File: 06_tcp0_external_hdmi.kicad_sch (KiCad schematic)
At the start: 27 parts, among them J30 External HDMI-A from TCP0, U50 TPD4E02B04DQA HDMI2.0 TMDS ES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, U51 TPD4E02B04DQA HDMI2.0 TMDS ES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, U52 TPD4E02B04DQA HDMI sideband E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

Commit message: Publish the current Ducktop2 design
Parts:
- removed F150: 100mA HDMI 5V detect fuse, Fuse:Fuse_1206_3216Metric, symbol Device:Fuse
- removed U51: TPD4E02B04DQA HDMI2.0 TMDS ESD B, Package_SON:USON-10_2.5x1.0mm_P0.5mm, symbol Power_Protection:TPD4E02B04DQA
- removed U52: TPD4E02B04DQA HDMI sideband ESD, Package_SON:USON-10_2.5x1.0mm_P0.5mm, symbol Power_Protection:TPD4E02B04DQA
- added C156, C157: 100n 16V HDMI AC coupling, Capacitor_SMD:C_0402_1005Metric, symbol Device:C
- added C159: 1u 10V X7R HDMI 5V switch output, Capacitor_SMD:C_0805_2012Metric, symbol Device:C
- added C160: 100p PCA9306 VREF2/EN filter, Capacitor_SMD:C_0402_1005Metric, symbol Device:C
- added C161: 100n HPD buffer local, Capacitor_SMD:C_0402_1005Metric, symbol Device:C
- added C162: 100n 10V X7R HDMI 5V switch input HF, Capacitor_SMD:C_0402_1005Metric, symbol Device:C
- added C163: 100n 10V X7R HDMI 5V switch output HF, Capacitor_SMD:C_0402_1005Metric, symbol Device:C
- added C164: 4.7n HDMI 5V switch rise-time, Capacitor_SMD:C_0402_1005Metric, symbol Device:C
- added C165: 4.7n HDMI 3V3 switch rise-time, Capacitor_SMD:C_0402_1005Metric, symbol Device:C
- added D155, D156, D157: TPD1E0B04DPLR HDMI TMDS ESD (0.15pF max), Diode_SMD:D_0201_0603Metric, symbol Device:D_TVS
- added Q50: BSS138 HDMI bias gate, Package_TO_SOT_SMD:SOT-23, symbol Q_NMOS_SOT23_GSD:Q_NMOS_SOT23_GSD
- added R156, R157: 470R 1% HDMI bias, Resistor_SMD:R_0402_1005Metric, symbol Device:R
- added R163: 1k HPD input series, Resistor_SMD:R_0402_1005Metric, symbol Device:R
- added R164: 100k HPD input pull-down, Resistor_SMD:R_0402_1005Metric, symbol Device:R
- added R165: 2.2k S0 bias-gate series, Resistor_SMD:R_0402_1005Metric, symbol Device:R
- added R166: 100k bias-gate default off, Resistor_SMD:R_0402_1005Metric, symbol Device:R
- added R167: 0R DNP HDMI bias always-on option, Resistor_SMD:R_0402_1005Metric, symbol Device:R
- added R168: 100k HDMI switched 5V discharge, Resistor_SMD:R_0402_1005Metric, symbol Device:R
- added R169: 100k HDMI switched 3V3 discharge, Resistor_SMD:R_0402_1005Metric, symbol Device:R
- added R570, R571, R572, R573, R574, R575, R576, R577, R578, R579: 75R 1% unused TPD13S523 channel termination, Resistor_SMD:R_0402_1005Metric, symbol Device:R
- added U50: TPD13S523PWR HDMI control ESD / 5V switch, Package_SO:TSSOP-16_4.4x5mm_P0.65mm, symbol TPD13S523PWR:TPD13S523PWR
- added U51: PCA9306DCTR HDMI DDC level translator, Package_SO:SSOP-8_2.95x2.8mm_P0.65mm, symbol PCA9306DCTR:PCA9306DCTR
- added U53: SN74LVC1G17DBVR HDMI HPD buffer, Package_TO_SOT_SMD:SOT-23-5, symbol 74xGxx:74LVC1G17
- added U54: TPS22975NDSGR host-active SYS_5V switch, Package_SON:Texas_DSG0008A_WSON-8-1EP_2x2mm_P0.5mm_EP0.9x1.6mm, symbol TPS22975N:TPS22975N
- added U55: TPS22975NDSGR host-active SYS_3V3 switch, Package_SON:Texas_DSG0008A_WSON-8-1EP_2x2mm_P0.5mm_EP0.9x1.6mm, symbol TPS22975N:TPS22975N
- C150: value 100n HDMI AC cap -> 100n 16V HDMI AC coupling; footprint Capacitor_SMD:C_0603_1608Metric -> Capacitor_SMD:C_0402_1005Metric; MPN (none) -> GRM155R71C104KA88D; Manufacturer (none) -> Murata
- C151: renamed from R151; value 470R HDMI bias per Mu ref -> 100n 16V HDMI AC coupling; footprint Resistor_SMD:R_0603_1608Metric -> Capacitor_SMD:C_0402_1005Metric; symbol Device:R -> Device:C; MPN (none) -> GRM155R71C104KA88D; Manufacturer (none) -> Murata
- C152: renamed from C153; value 100n HDMI AC cap -> 100n 16V HDMI AC coupling; footprint Capacitor_SMD:C_0603_1608Metric -> Capacitor_SMD:C_0402_1005Metric; MPN (none) -> GRM155R71C104KA88D; Manufacturer (none) -> Murata
- C153: renamed from R154; value 470R HDMI bias per Mu ref -> 100n 16V HDMI AC coupling; footprint Resistor_SMD:R_0603_1608Metric -> Capacitor_SMD:C_0402_1005Metric; symbol Device:R -> Device:C; MPN (none) -> GRM155R71C104KA88D; Manufacturer (none) -> Murata
- C154: renamed from C156; value 100n HDMI AC cap -> 100n 16V HDMI AC coupling; footprint Capacitor_SMD:C_0603_1608Metric -> Capacitor_SMD:C_0402_1005Metric; MPN (none) -> GRM155R71C104KA88D; Manufacturer (none) -> Murata
- C155: renamed from R157; value 470R HDMI bias per Mu ref -> 100n 16V HDMI AC coupling; footprint Resistor_SMD:R_0603_1608Metric -> Capacitor_SMD:C_0402_1005Metric; symbol Device:R -> Device:C; MPN (none) -> GRM155R71C104KA88D; Manufacturer (none) -> Murata
- C158: value 1u HDMI 5V -> 1u 10V X7R HDMI 5V switch input; MPN (none) -> GRM188R71A105KA61D; Manufacturer (none) -> Murata
- D150: renamed from C151; value 100n HDMI AC cap -> TPD1E0B04DPLR HDMI TMDS ESD (0.15pF max); footprint Capacitor_SMD:C_0603_1608Metric -> Diode_SMD:D_0201_0603Metric; symbol Device:C -> Device:D_TVS; MPN (none) -> TPD1E0B04DPLR; Manufacturer (none) -> Texas Instruments
- D151: renamed from R152; value 470R HDMI bias per Mu ref -> TPD1E0B04DPLR HDMI TMDS ESD (0.15pF max); footprint Resistor_SMD:R_0603_1608Metric -> Diode_SMD:D_0201_0603Metric; symbol Device:R -> Device:D_TVS; MPN (none) -> TPD1E0B04DPLR; Manufacturer (none) -> Texas Instruments
- D152: renamed from C154; value 100n HDMI AC cap -> TPD1E0B04DPLR HDMI TMDS ESD (0.15pF max); footprint Capacitor_SMD:C_0603_1608Metric -> Diode_SMD:D_0201_0603Metric; symbol Device:C -> Device:D_TVS; MPN (none) -> TPD1E0B04DPLR; Manufacturer (none) -> Texas Instruments
- D153: renamed from R155; value 470R HDMI bias per Mu ref -> TPD1E0B04DPLR HDMI TMDS ESD (0.15pF max); footprint Resistor_SMD:R_0603_1608Metric -> Diode_SMD:D_0201_0603Metric; symbol Device:R -> Device:D_TVS; MPN (none) -> TPD1E0B04DPLR; Manufacturer (none) -> Texas Instruments
- D154: renamed from C157; value 100n HDMI AC cap -> TPD1E0B04DPLR HDMI TMDS ESD (0.15pF max); footprint Capacitor_SMD:C_0603_1608Metric -> Diode_SMD:D_0201_0603Metric; symbol Device:C -> Device:D_TVS; MPN (none) -> TPD1E0B04DPLR; Manufacturer (none) -> Texas Instruments
- J30: MPN (none) -> 208658-1001; Manufacturer (none) -> Molex
- R150: value 470R HDMI bias per Mu ref -> 470R 1% HDMI bias; footprint Resistor_SMD:R_0603_1608Metric -> Resistor_SMD:R_0402_1005Metric; MPN (none) -> RC0402FR-07470RL; Manufacturer (none) -> Yageo
- R151: renamed from C152; value 100n HDMI AC cap -> 470R 1% HDMI bias; footprint Capacitor_SMD:C_0603_1608Metric -> Resistor_SMD:R_0402_1005Metric; symbol Device:C -> Device:R; MPN (none) -> RC0402FR-07470RL; Manufacturer (none) -> Yageo
- R152: renamed from R153; value 470R HDMI bias per Mu ref -> 470R 1% HDMI bias; footprint Resistor_SMD:R_0603_1608Metric -> Resistor_SMD:R_0402_1005Metric; MPN (none) -> RC0402FR-07470RL; Manufacturer (none) -> Yageo
- R153: renamed from C155; value 100n HDMI AC cap -> 470R 1% HDMI bias; footprint Capacitor_SMD:C_0603_1608Metric -> Resistor_SMD:R_0402_1005Metric; symbol Device:C -> Device:R; MPN (none) -> RC0402FR-07470RL; Manufacturer (none) -> Yageo
- R154: renamed from R156; value 470R HDMI bias per Mu ref -> 470R 1% HDMI bias; footprint Resistor_SMD:R_0603_1608Metric -> Resistor_SMD:R_0402_1005Metric; MPN (none) -> RC0402FR-07470RL; Manufacturer (none) -> Yageo
- R155: renamed from U50; value TPD4E02B04DQA HDMI2.0 TMDS ESD A -> 470R 1% HDMI bias; footprint Package_SON:USON-10_2.5x1.0mm_P0.5mm -> Resistor_SMD:R_0402_1005Metric; symbol Power_Protection:TPD4E02B04DQA -> Device:R; MPN (none) -> RC0402FR-07470RL; Manufacturer (none) -> Yageo
- R158: value 2.2k HDMI DDC SCL pull-up -> 2.2k HDMI DDC pull-up; footprint Resistor_SMD:R_0603_1608Metric -> Resistor_SMD:R_0402_1005Metric; MPN (none) -> RC0402FR-072K2L; Manufacturer (none) -> Yageo
- R159: value 2.2k HDMI DDC SDA pull-up -> 2.2k HDMI DDC pull-up; footprint Resistor_SMD:R_0603_1608Metric -> Resistor_SMD:R_0402_1005Metric; MPN (none) -> RC0402FR-072K2L; Manufacturer (none) -> Yageo
- R160: value 100R HPD series -> 1.8k HDMI DDC pull-up; footprint Resistor_SMD:R_0603_1608Metric -> Resistor_SMD:R_0402_1005Metric; MPN (none) -> RC0402FR-071K8L; Manufacturer (none) -> Yageo
- R161: value 100R DDC SCL series -> 1.8k HDMI DDC pull-up; footprint Resistor_SMD:R_0603_1608Metric -> Resistor_SMD:R_0402_1005Metric; MPN (none) -> RC0402FR-071K8L; Manufacturer (none) -> Yageo
- R162: value 100R DDC SDA series -> 200k PCA9306 VREF2/EN bias; footprint Resistor_SMD:R_0603_1608Metric -> Resistor_SMD:R_0402_1005Metric; MPN (none) -> RC0402FR-07200KL; Manufacturer (none) -> Yageo
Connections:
- net EXT_HDMI_5V: now also R160.1, R161.1, R162.1, C159.1, C163.1, U50.6 (5V_OUT); no longer C158.1, R158.1, R159.1
- net EXT_HDMI_CK_N: now also C157.2, D157.1 (A1), R157.1; no longer C155.1, D154.2
- net EXT_HDMI_CK_P: now also C156.2, D156.1 (A1), R156.1; no longer C154.2, R154.1
- net EXT_HDMI_D0_N: now also C155.2, R155.1, D155.1 (A1); no longer D153.1, R153.2
- net EXT_HDMI_D0_P: now also C154.2, D154.1 (A1), R154.1; no longer C153.1, D152.2
- net EXT_HDMI_D1_N: now also C153.2, D153.1 (A1), R153.1; no longer C152.2, R152.1, R155.5 (IO4)
- net EXT_HDMI_D1_P: now also C152.2, D152.1 (A1), R152.1; no longer D151.1, R151.2, R155.4 (IO3)
- net EXT_HDMI_D2_N: now also C151.2, D151.1 (A1), R151.1; no longer C151.1, D150.2, R155.2 (IO2)
- net EXT_HDMI_D2_P: now also D150.1 (A1); no longer R155.1 (IO1)
- net EXT_HDMI_HPD_CONN: now also R163.1, U50.3 (CTRL3); no longer R160.2
- net EXT_HDMI_SCL_CONN: now also R160.2, U50.1 (CTRL1), U51.6 (SCL2); no longer R158.2, R161.2
- net EXT_HDMI_SDA_CONN: now also R161.2, U50.2 (CTRL2), U51.5 (SDA2); no longer R159.2, R162.2
- net GND: now also D150.2 (A2), D152.2 (A2), D154.2 (A2), C159.2, C160.2, C161.2, C162.2, C163.2, C164.2, C165.2, D155.2 (A2), D156.2 (A2), D157.2 (A2), Q50.2 (S), R164.2, R166.2, R167.2, R168.2, R169.2, R570.2, R571.2, R572.2, R573.2, R574.2, R575.2, R576.2, R577.2, R578.2, R579.2, U50.8 (GND), U51.1 (GND), U53.3 (GND), U54.5 (GND), U54.9 (EP), U55.5 (GND), U55.9 (EP); no longer C151.2, C153.2, C155.2, R150.2, R152.2, R154.2, R155.3 (G), R155.8 (G)
- net SYS_5V: now also U54.1 (VIN), U54.2 (VIN), U54.4 (VBIAS)
- net TCP0_DDC_SCL: now also R158.2, U51.3 (SCL1); no longer R161.1
- net TCP0_DDC_SDA: now also R159.2, U51.4 (SDA1); no longer R162.1
- net TCP0_HPD: now also U53.4; no longer R160.1
- net TCP0_TX0_N: now also C151.1; no longer R153.1
- net TCP0_TX0_P: now also C150.1; no longer D152.1
- net TCP0_TX1_N: now also C155.1; no longer C152.1
- net TCP0_TX1_P: now also C154.1; no longer R151.1
- net TCP0_TXRX0_N: now also C153.1; no longer D150.1
- net TCP0_TXRX0_P: now also C152.1; no longer C150.1
- net TCP0_TXRX1_N: now also C157.1; no longer D154.1
- net TCP0_TXRX1_P: now also C156.1; no longer C154.1
- net EXT_HDMI_CEC: no longer names the net of J30.13 (CEC)
- new net EXT_HDMI_BIAS_GATE: Q50.1 (G), R165.2, R166.1
- new net EXT_HDMI_BIAS_RETURN: Q50.3 (D), R150.2, R151.2, R152.2, R153.2, R154.2, R155.2, R156.2, R157.2, R167.1
- new net EXT_HDMI_HPD_NODE: R163.2, R164.1, U53.2
- new net HDMI_3V3_SWITCH_CT: C165.1, U55.6 (CT)
- new net HDMI_5V_SWITCH_CT: C164.1, U54.6 (CT)
- new net HDMI_DDC_REF5: C160.1, R162.2, U51.7 (VREF2), U51.8 (EN)
- new net HDMI_HOST_3V3: C161.1, R158.1, R159.1, R169.1, U51.2 (VREF1), U53.5 (VCC), U55.7 (VOUT), U55.8 (VOUT)
- new net HDMI_SOURCE_5V: C158.1, C162.1, R168.1, U50.5 (5V_SUPPLY), U54.7 (VOUT), U54.8 (VOUT)
- new net HDMI_TPD_D0_UNUSED: R570.1, U50.4 (CTRL4)
- new net HDMI_TPD_D1_UNUSED: R571.1, U50.7 (CTRL5)
- new net HDMI_TPD_D2_UNUSED: R572.1, U50.9 (D3-)
- new net HDMI_TPD_D3_UNUSED: R573.1, U50.10 (D3+)
- new net HDMI_TPD_D4_UNUSED: R574.1, U50.11 (D2-)
- new net HDMI_TPD_D5_UNUSED: R575.1, U50.12 (D2+)
- new net HDMI_TPD_D6_UNUSED: R576.1, U50.13 (D1-)
- new net HDMI_TPD_D7_UNUSED: R577.1, U50.14 (D1+)
- new net HDMI_TPD_D8_UNUSED: R578.1, U50.15 (D0-)
- new net HDMI_TPD_D9_UNUSED: R579.1, U50.16 (D0+)
- new net MU_HOST_ACTIVE: R165.1, U54.3 (ON), U55.3 (ON)
- new net SYS_3V3: U55.1 (VIN), U55.2 (VIN), U55.4 (VBIAS)
- no-connect marks 13 -> 3
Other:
- note added: "CEC and utility are explicitly NC; unused TPD13S523 legacy channels use the datasheet 75R-to-GND termination."
- note added: "J30 is the outside-world HDMI jack. The retired Intehill controller is a bench-test/fallback fixture, not motherboard circuitry."
- note added: "Lane map, AC coupling, bias gating, DDC/HPD translation, and 5V isolation follow the Mu reference."
- note added: "LattePanda Mu default BIOS maps TCP0 as HDMI 2.0; the internal panel uses the Mu module's onboard eDP connector."
- note added: "Release gate: verify >=4.8V at J30 pin 18 under 55mA and validate the finished 100-ohm HDMI 2.0 layout on hardware."
- note added: "TMDS ESD uses 0.15pF-max, +/-3.6V TPD1E0B04DPLR single-line parts; route each shunt at J30 with no stub."
- note added: "U54/U55 remove 5V/DDC/HPD power while the Mu is off; PCA9306 translates DDC/SCDC and U53 buffers HPD."
- note removed: "CEC is ESD-protected but not connected to the Mu or EC in this pass."
- note removed: "J30 is the outside-world HDMI jack; sheet 11 J300 remains only the internal Intehill HDMI plug."
- note removed: "LattePanda Mu default BIOS maps TCP0 as HDMI 2.0; DDIB remains the internal Intehill display."
- note removed: "Pre-layout must verify TCP0 HDMI lane order/polarity against the selected Mu BIOS/reference design."
- note removed: "TCP1 remains the better future candidate for a Type-C video/PD port if a later BIOS/display plan needs it."
- note removed: "This sheet is the user-accessible external HDMI-A connector for a second monitor."
- note removed: "Treat this as HDMI 2.0/18Gbps capable: short routing, low-cap ESD, solid return path, no HDMI 1.4-only parts."
- moved on the sheet: C152, C154, R152, R154

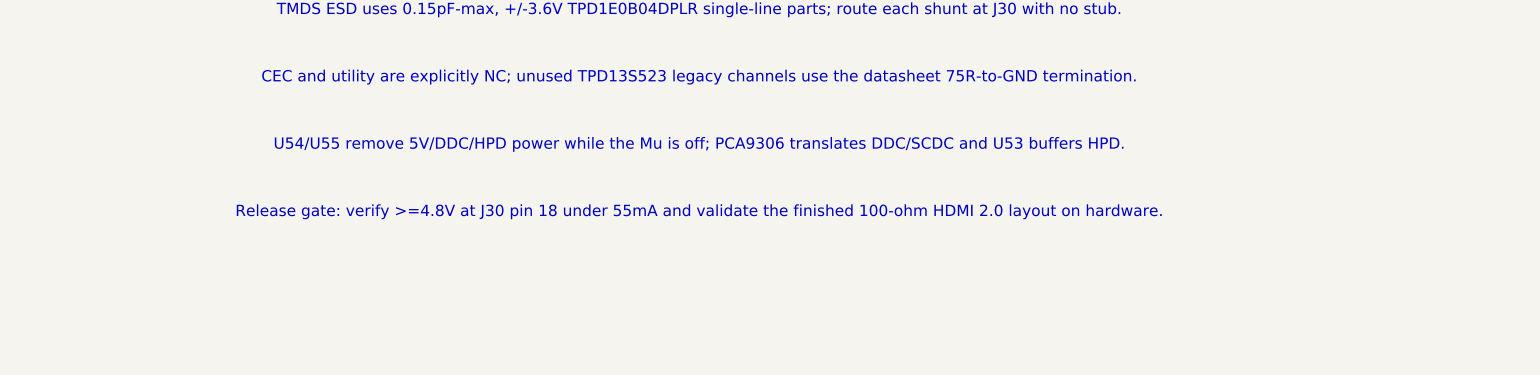
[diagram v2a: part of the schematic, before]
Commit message: Refresh repository with updated PCB renders and current design state
- New 3D renders: top, bottom, perspective, and keyboard PCB
  (generated via kicad-cli 10.0.4, 2560x1440, high quality)
- Update README status: placement complete, coupling caps relocated,
  independent design review CONDITIONAL PASS (2026-07-21)
- Add keyboard rev-A fullboard stencil generation (3MF, STL, manifest, script)
- Track TPS3897ADRYR library symbol
- WIP schematic, PCB, and generator refinements post-coupling-cap fix
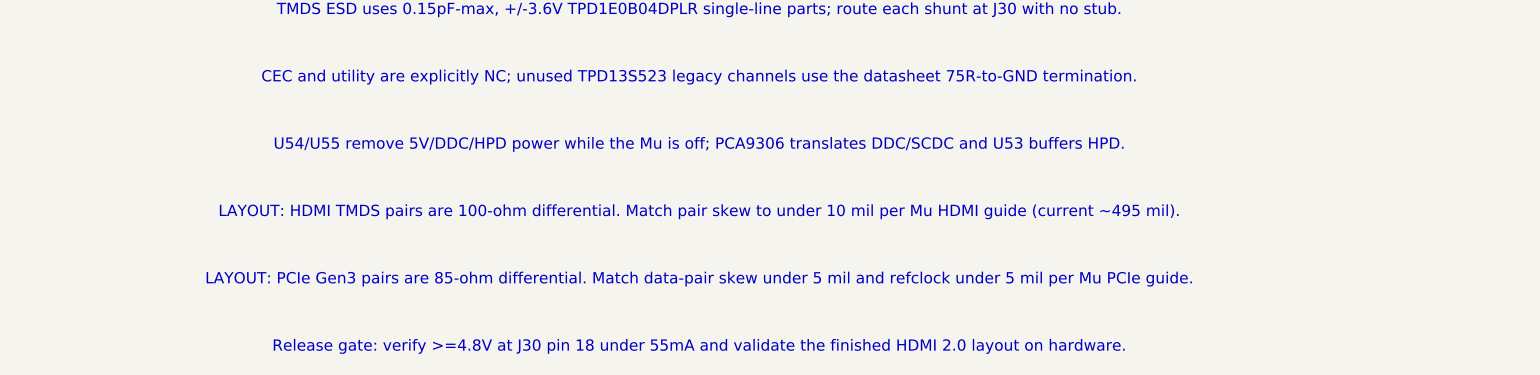
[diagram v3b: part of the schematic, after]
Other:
- note added: "LAYOUT: HDMI TMDS pairs are 100-ohm differential. Match pair skew to under 10 mil per Mu HDMI guide (current ~495 mil)."
- note added: "LAYOUT: PCIe Gen3 pairs are 85-ohm differential. Match data-pair skew under 5 mil and refclock under 5 mil per Mu PCIe guide."
- note added: "Release gate: verify >=4.8V at J30 pin 18 under 55mA and validate the finished HDMI 2.0 layout on hardware."
- note removed: "Release gate: verify >=4.8V at J30 pin 18 under 55mA and validate the finished 100-ohm HDMI 2.0 layout on hardware."
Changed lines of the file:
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@@
 (text "CEC and utility are explicitly NC; unused TPD13S523 legacy channels use the datasheet 75R-to-GND termination." (at 20.32 251.46 0) (effects (font (size 1.27 1.27))))
 (text "U54/U55 remove 5V/DDC/HPD power while the Mu is off; PCA9306 translates DDC/SCDC and U53 buffers HPD." (at 20.32 259.08 0) (effects (font (size 1.27 1.27))))
-(text "Release gate: verify >=4.8V at J30 pin 18 under 55mA and validate the finished 100-ohm HDMI 2.0 layout on hardware." (at 20.32 266.7 0) (effects (font (size 1.27 1.27))))
+(text "LAYOUT: HDMI TMDS pairs are 100-ohm differential. Match pair skew to under 10 mil per Mu HDMI guide (current ~495 mil)." (at 20.32 266.7 0) (effects (font (size 1.27 1.27))))
+(text "LAYOUT: PCIe Gen3 pairs are 85-ohm differential. Match data-pair skew under 5 mil and refclock under 5 mil per Mu PCIe guide." (at 20.32 274.32 0) (effects (font (size 1.27 1.27))))
+(text "Release gate: verify >=4.8V at J30 pin 18 under 55mA and validate the finished HDMI 2.0 layout on hardware." (at 20.32 281.94 0) (effects (font (size 1.27 1.27))))
 (sheet_instances
   (path "/f0ae9354-2124-5719-9bb0-6fdcc1f0d78d"

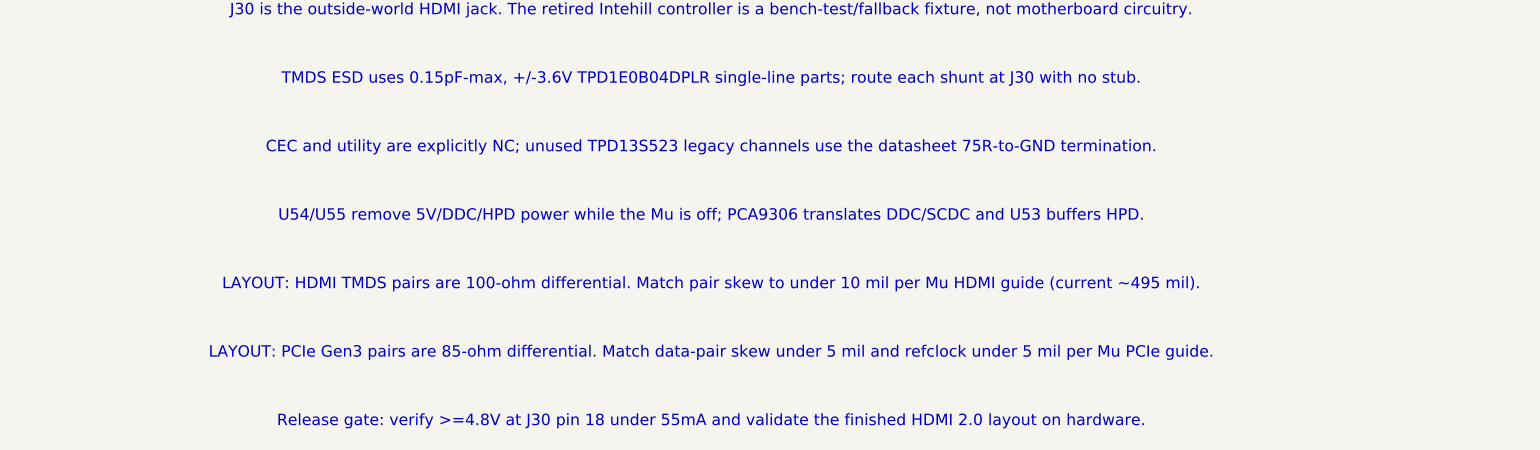
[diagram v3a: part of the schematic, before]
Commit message: Wire the trackpad directly over USB2 and record audit holds
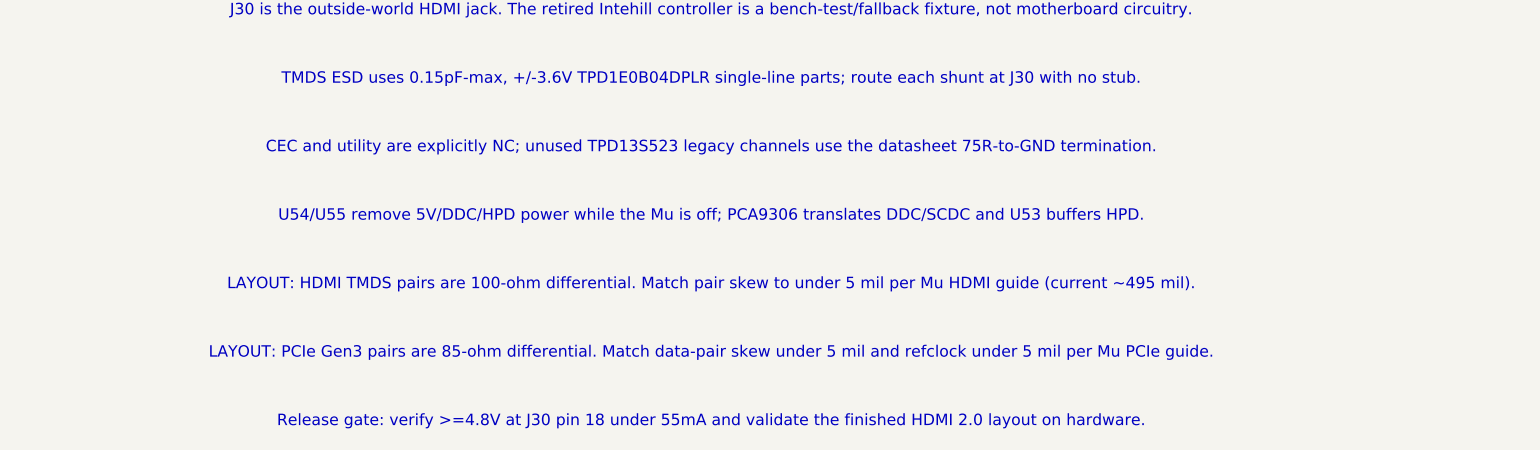
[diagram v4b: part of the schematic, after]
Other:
- note added: "LAYOUT: HDMI TMDS pairs are 100-ohm differential. Match pair skew to under 5 mil per Mu HDMI guide (current ~495 mil)."
- note removed: "LAYOUT: HDMI TMDS pairs are 100-ohm differential. Match pair skew to under 10 mil per Mu HDMI guide (current ~495 mil)."
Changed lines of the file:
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@@
 (text "CEC and utility are explicitly NC; unused TPD13S523 legacy channels use the datasheet 75R-to-GND termination." (at 20.32 251.46 0) (effects (font (size 1.27 1.27))))
 (text "U54/U55 remove 5V/DDC/HPD power while the Mu is off; PCA9306 translates DDC/SCDC and U53 buffers HPD." (at 20.32 259.08 0) (effects (font (size 1.27 1.27))))
-(text "LAYOUT: HDMI TMDS pairs are 100-ohm differential. Match pair skew to under 10 mil per Mu HDMI guide (current ~495 mil)." (at 20.32 266.7 0) (effects (font (size 1.27 1.27))))
+(text "LAYOUT: HDMI TMDS pairs are 100-ohm differential. Match pair skew to under 5 mil per Mu HDMI guide (current ~495 mil)." (at 20.32 266.7 0) (effects (font (size 1.27 1.27))))
 (text "LAYOUT: PCIe Gen3 pairs are 85-ohm differential. Match data-pair skew under 5 mil and refclock under 5 mil per Mu PCIe guide." (at 20.32 274.32 0) (effects (font (size 1.27 1.27))))
 (text "Release gate: verify >=4.8V at J30 pin 18 under 55mA and validate the finished HDMI 2.0 layout on hardware." (at 20.32 281.94 0) (effects (font (size 1.27 1.27))))

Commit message: Assign 327 BOM MPNs across 11 schematic sheets (370→43 gaps)
Closes 370 BOM procurement gaps by assigning Yageo resistor and Murata
capacitor MPNs to all passive components in the project's 11 schematic
sheets. 43 intentional holds remain for design-review items (crystal
loads, audio AC-coupling, VCAP, C0G timing, maker MCU 4.7u 0402s).

Key changes:
- 205 resistors assigned (Yageo RC0603/RT0603 series)
- 124 capacitors assigned (Murata GRM series, matching footprint body size)
- Fixed C183: 4.7u MPN→1u (GRM21BR71A105KA01L)
- Fixed C795/C840: upgraded to 50V rating (GRM21BR71H105KA12L)
- Generated fresh inventory: 1173 components, 43 remaining gaps
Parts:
- C164, C165: MPN (none) -> GRM155R71C472KA01D; Manufacturer (none) -> Murata
- R164, R166, R168, R169: MPN (none) -> RC0402FR-07100KL; Manufacturer (none) -> Yageo
- R165: MPN (none) -> RC0402FR-072K2L; Manufacturer (none) -> Yageo
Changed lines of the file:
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@@
   (property "Footprint" "Resistor_SMD:R_0402_1005Metric" (at 529.59 177.8 0) (effects (font (size 1.27 1.27)) (hide yes)))
   (property "Datasheet" "" (at 529.59 177.8 0) (effects (font (size 1.27 1.27)) (hide yes)))
+  (property "Manufacturer" "Yageo" (at 529.59 177.8 0) (effects (font (size 1.27 1.27)) (hide yes)))
+  (property "MPN" "RC0402FR-072K2L" (at 529.59 177.8 0) (effects (font (size 1.27 1.27)) (hide yes)))
   (pin "1")
   (pin "2")
@@
   (property "Footprint" "Resistor_SMD:R_0402_1005Metric" (at 529.59 190.5 0) (effects (font (size 1.27 1.27)) (hide yes)))
   (property "Datasheet" "" (at 529.59 190.5 0) (effects (font (size 1.27 1.27)) (hide yes)))
+  (property "Manufacturer" "Yageo" (at 529.59 190.5 0) (effects (font (size 1.27 1.27)) (hide yes)))
+  (property "MPN" "RC0402FR-07100KL" (at 529.59 190.5 0) (effects (font (size 1.27 1.27)) (hide yes)))
   (pin "1")
   (pin "2")
@@
   (property "Footprint" "Capacitor_SMD:C_0402_1005Metric" (at 454.66 38.1 0) (effects (font (size 1.27 1.27)) (hide yes)))
   (property "Datasheet" "" (at 454.66 38.1 0) (effects (font (size 1.27 1.27)) (hide yes)))
+  (property "Manufacturer" "Murata" (at 454.66 38.1 0) (effects (font (size 1.27 1.27)) (hide yes)))
+  (property "MPN" "GRM155R71C472KA01D" (at 454.66 38.1 0) (effects (font (size 1.27 1.27)) (hide yes)))
   (pin "1")
   (pin "2")
@@
   (property "Footprint" "Capacitor_SMD:C_0402_1005Metric" (at 454.66 101.6 0) (effects (font (size 1.27 1.27)) (hide yes)))
   (property "Datasheet" "" (at 454.66 101.6 0) (effects (font (size 1.27 1.27)) (hide yes)))
+  (property "Manufacturer" "Murata" (at 454.66 101.6 0) (effects (font (size 1.27 1.27)) (hide yes)))
+  (property "MPN" "GRM155R71C472KA01D" (at 454.66 101.6 0) (effects (font (size 1.27 1.27)) (hide yes)))
   (pin "1")
   (pin "2")
@@
   (property "Footprint" "Resistor_SMD:R_0402_1005Metric" (at 454.66 50.8 0) (effects (font (size 1.27 1.27)) (hide yes)))
   (property "Datasheet" "" (at 454.66 50.8 0) (effects (font (size 1.27 1.27)) (hide yes)))
+  (property "Manufacturer" "Yageo" (at 454.66 50.8 0) (effects (font (size 1.27 1.27)) (hide yes)))
+  (property "MPN" "RC0402FR-07100KL" (at 454.66 50.8 0) (effects (font (size 1.27 1.27)) (hide yes)))
   (pin "1")
   (pin "2")
@@
   (property "Footprint" "Resistor_SMD:R_0402_1005Metric" (at 454.66 114.3 0) (effects (font (size 1.27 1.27)) (hide yes)))
   (property "Datasheet" "" (at 454.66 114.3 0) (effects (font (size 1.27 1.27)) (hide yes)))
+  (property "Manufacturer" "Yageo" (at 454.66 114.3 0) (effects (font (size 1.27 1.27)) (hide yes)))
+  (property "MPN" "RC0402FR-07100KL" (at 454.66 114.3 0) (effects (font (size 1.27 1.27)) (hide yes)))
   (pin "1")
   (pin "2")
@@
   (property "Footprint" "Resistor_SMD:R_0402_1005Metric" (at 650.24 132.08 0) (effects (font (size 1.27 1.27)) (hide yes)))
   (property "Datasheet" "" (at 650.24 132.08 0) (effects (font (size 1.27 1.27)) (hide yes)))
-  (pin "1")
-  (pin "2")
+  (property "Manufacturer" "Yageo" (at 650.24 132.08 0) (effects (font (size 1.27 1.27)) (hide yes)))
+  (property "MPN" "RC0402FR-07100KL" (at 650.24 132.08 0) (effects (font (size 1.27 1.27)) (hide yes)))
+  (pin "1")
+  (pin "2")
